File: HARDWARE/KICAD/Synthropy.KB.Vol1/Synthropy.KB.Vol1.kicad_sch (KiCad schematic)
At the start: 1 part, among them U1 kb2040

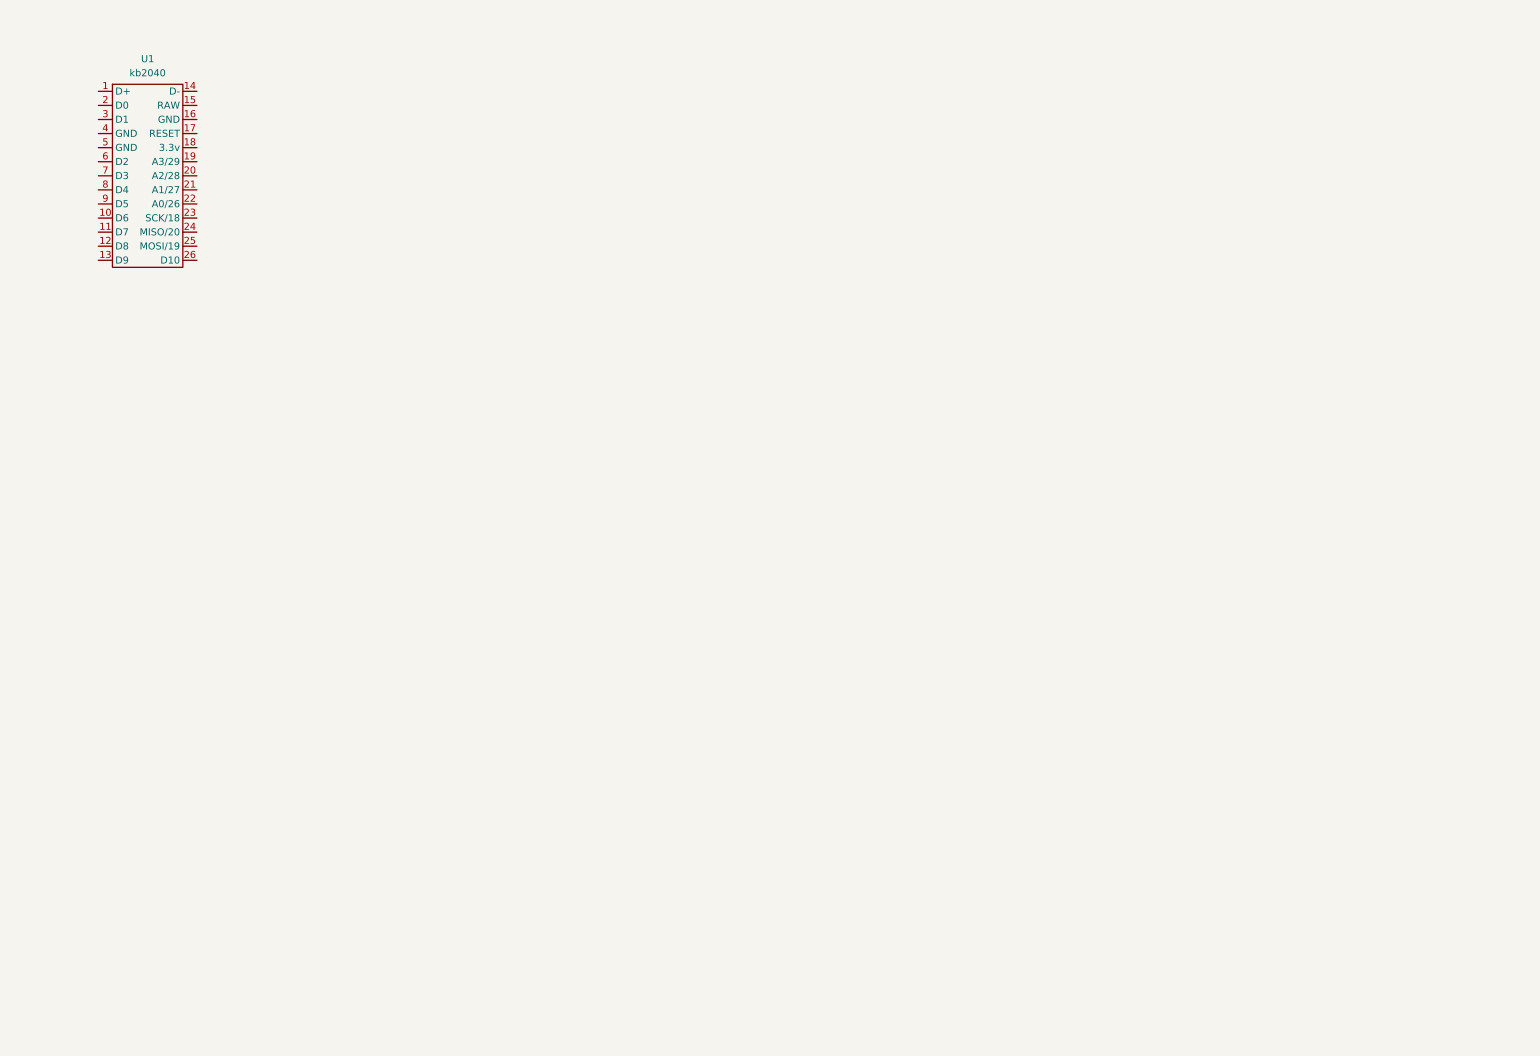
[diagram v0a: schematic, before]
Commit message: Schematic Updates
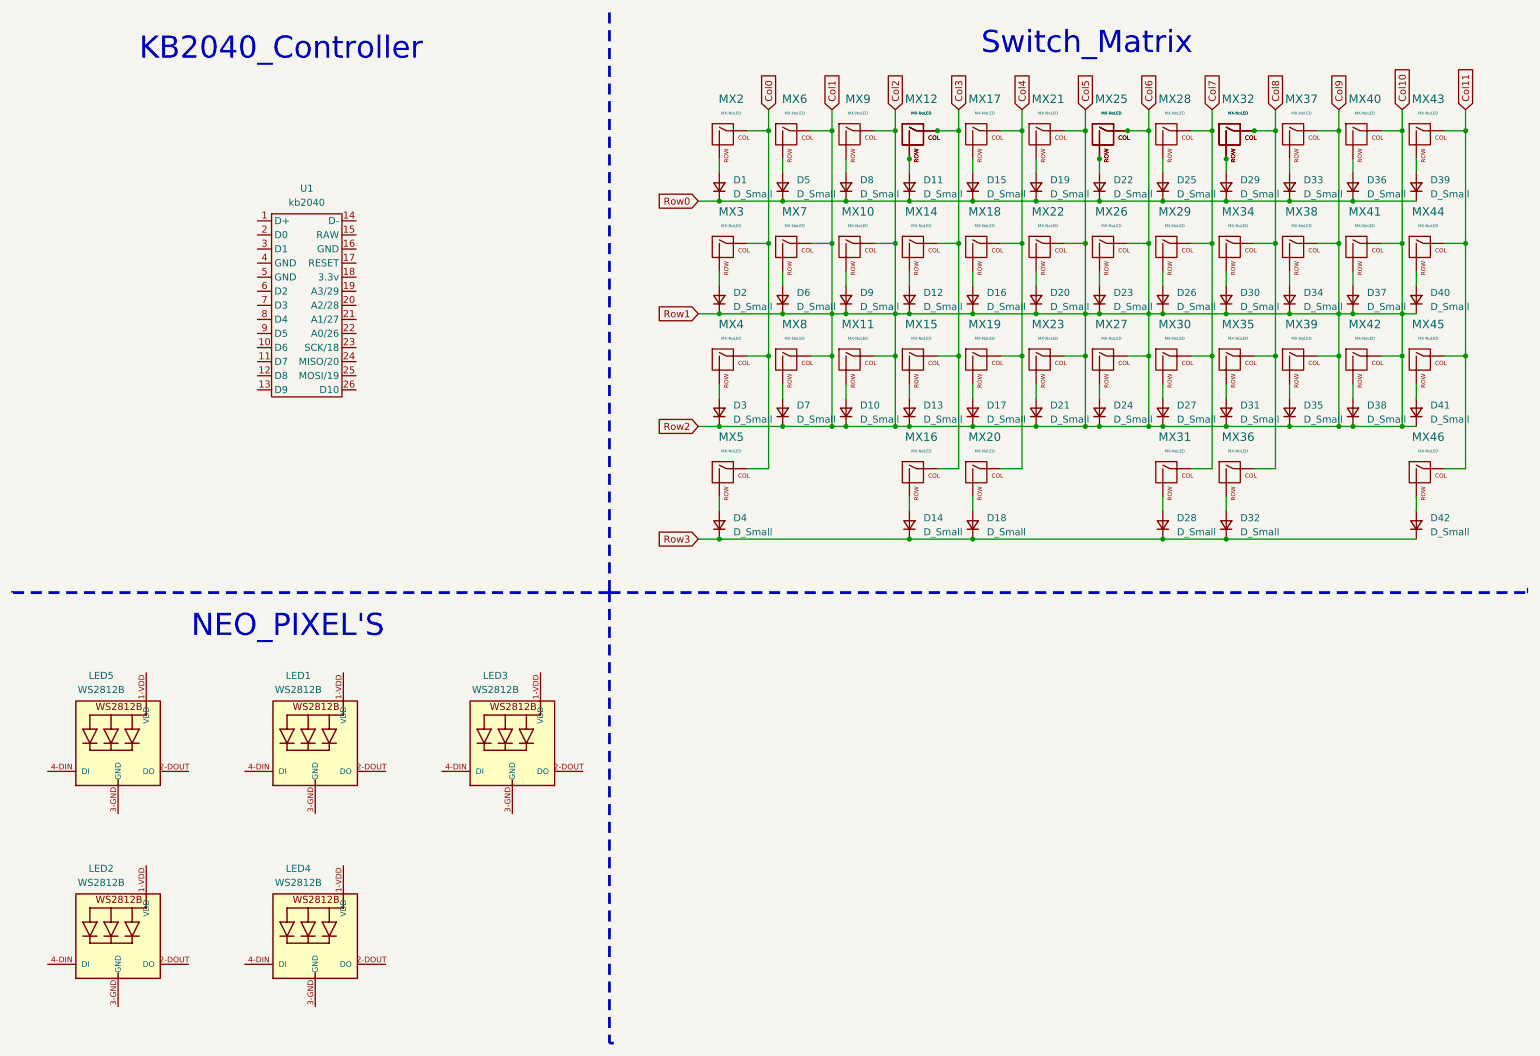
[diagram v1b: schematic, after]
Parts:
- added D1, D10, D11, D12, D13, D14, D15, D16, D17, D18, D19, D2, D20, D21, D22, D23, D24, D25, D26, D27, D28, D29, D3, D30, D31, D32, D33, D34, D35, D36, D37, D38, D39, D4, D40, D41, D42, D5, D6, D7, D8, D9: D_Small, Diode_SMD:D_SOD-123, symbol Device:D_Small
- added LED1, LED2, LED3, LED4, LED5: WS2812B, symbol WS2812B:WS2812B
- added MX10, MX11, MX12, MX13, MX14, MX15, MX16, MX17, MX18, MX19, MX2, MX20, MX21, MX22, MX23, MX24, MX25, MX26, MX27, MX28, MX29, MX3, MX30, MX31, MX32, MX33, MX34, MX35, MX36, MX37, MX38, MX39, MX4, MX40, MX41, MX42, MX43, MX44, MX45, MX46, MX5, MX6, MX7, MX8, MX9: MX-NoLED, Kailh_Switch:Kailh_Choc_SP, symbol MX_Alps_Hybrid:MX-NoLED
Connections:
- new net: D15.2 (A), MX17.2 (ROW)
- new net: D6.2 (A), MX7.2 (ROW)
- new net: D7.2 (A), MX8.2 (ROW)
- new net: D27.2 (A), MX30.2 (ROW)
- new net: D18.2 (A), MX20.2 (ROW)
- new net: D39.2 (A), MX43.2 (ROW)
- new net: D2.2 (A), MX3.2 (ROW)
- new net: D5.2 (A), MX6.2 (ROW)
- new net: D37.2 (A), MX41.2 (ROW)
- new net: D30.2 (A), MX34.2 (ROW)
- new net: D28.2 (A), MX31.2 (ROW)
- new net: D3.2 (A), MX4.2 (ROW)
- new net: D33.2 (A), MX37.2 (ROW)
- new net: D34.2 (A), MX38.2 (ROW)
- new net: D16.2 (A), MX18.2 (ROW)
- new net: D38.2 (A), MX42.2 (ROW)
- new net: D40.2 (A), MX44.2 (ROW)
- new net: D17.2 (A), MX19.2 (ROW)
- new net: D29.2 (A), MX32.2 (ROW), MX33.2 (ROW)
- new net: D11.2 (A), MX12.2 (ROW), MX13.2 (ROW)
- new net: D42.2 (A), MX46.2 (ROW)
- new net: D32.2 (A), MX36.2 (ROW)
- new net: D35.2 (A), MX39.2 (ROW)
- new net: D22.2 (A), MX24.2 (ROW), MX25.2 (ROW)
- new net: D26.2 (A), MX29.2 (ROW)
- new net: D4.2 (A), MX5.2 (ROW)
- new net: D12.2 (A), MX14.2 (ROW)
- new net: D20.2 (A), MX22.2 (ROW)
- new net: D9.2 (A), MX10.2 (ROW)
- new net: D8.2 (A), MX9.2 (ROW)
- new net: D41.2 (A), MX45.2 (ROW)
- new net: D36.2 (A), MX40.2 (ROW)
- new net: D13.2 (A), MX15.2 (ROW)
- new net: D31.2 (A), MX35.2 (ROW)
- new net: D24.2 (A), MX27.2 (ROW)
- new net: D1.2 (A), MX2.2 (ROW)
- new net: D10.2 (A), MX11.2 (ROW)
- new net: D14.2 (A), MX16.2 (ROW)
- new net: D19.2 (A), MX21.2 (ROW)
- new net: D25.2 (A), MX28.2 (ROW)
- new net: D21.2 (A), MX23.2 (ROW)
- new net: D23.2 (A), MX26.2 (ROW)
- new net Col0: MX2.1 (COL), MX3.1 (COL), MX4.1 (COL), MX5.1 (COL)
- new net Col1: D10.1 (K), D12.1 (K), D13.1 (K), D16.1 (K), D17.1 (K), D2.1 (K), D20.1 (K), D21.1 (K), D23.1 (K), D24.1 (K), D26.1 (K), D27.1 (K), D3.1 (K), D30.1 (K), D31.1 (K), D34.1 (K), D35.1 (K), D37.1 (K), D38.1 (K), D40.1 (K), D41.1 (K), D6.1 (K), D7.1 (K), D9.1 (K), MX10.1 (COL), MX11.1 (COL), MX21.1 (COL), MX22.1 (COL), MX23.1 (COL), MX24.1 (COL), MX25.1 (COL), MX26.1 (COL), MX27.1 (COL), MX37.1 (COL), MX38.1 (COL), MX39.1 (COL), MX40.1 (COL), MX41.1 (COL), MX42.1 (COL), MX6.1 (COL), MX7.1 (COL), MX8.1 (COL), MX9.1 (COL)
- new net Col11: MX43.1 (COL), MX44.1 (COL), MX45.1 (COL), MX46.1 (COL)
- new net Col3: MX12.1 (COL), MX13.1 (COL), MX14.1 (COL), MX15.1 (COL), MX16.1 (COL)
- new net Col4: MX17.1 (COL), MX18.1 (COL), MX19.1 (COL), MX20.1 (COL)
- new net Col7: MX28.1 (COL), MX29.1 (COL), MX30.1 (COL), MX31.1 (COL)
- new net Col8: MX32.1 (COL), MX33.1 (COL), MX34.1 (COL), MX35.1 (COL), MX36.1 (COL)
- new net Row0: D1.1 (K), D11.1 (K), D15.1 (K), D19.1 (K), D22.1 (K), D25.1 (K), D29.1 (K), D33.1 (K), D36.1 (K), D39.1 (K), D5.1 (K), D8.1 (K)
- new net Row3: D14.1 (K), D18.1 (K), D28.1 (K), D32.1 (K), D4.1 (K), D42.1 (K)
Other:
- note added: "KB2040_Controller"
- note added: "NEO_PIXEL'S"
- note added: "Switch_Matrix"
- moved on the sheet: U1

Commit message: Updates from prev revisions
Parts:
- removed MX12, MX25, MX33: MX-NoLED, Kailh_Switch:Kailh_Choc_SP, symbol MX_Alps_Hybrid:MX-NoLED
- LED1: renamed from LED5; footprint (none) -> Keebio-Parts.pretty-master:WS2812B
- LED2: renamed from LED3; footprint (none) -> Keebio-Parts.pretty-master:WS2812B
- LED3: renamed from LED2; footprint (none) -> Keebio-Parts.pretty-master:WS2812B
- LED4: footprint (none) -> Keebio-Parts.pretty-master:WS2812B
- LED5: renamed from LED1; footprint (none) -> Keebio-Parts.pretty-master:WS2812B
- MX1: renamed from MX2; footprint Kailh_Switch:Kailh_Choc_SP -> Switch_Keyboard_Kailh:SW_Kailh_Choc_V1V2_1.00u
- MX10: renamed from MX37; footprint Kailh_Switch:Kailh_Choc_SP -> Switch_Keyboard_Kailh:SW_Kailh_Choc_V1V2_1.00u
- MX11: renamed from MX40; footprint Kailh_Switch:Kailh_Choc_SP -> Switch_Keyboard_Kailh:SW_Kailh_Choc_V1V2_1.00u
- MX12: renamed from MX43; footprint Kailh_Switch:Kailh_Choc_SP -> Switch_Keyboard_Kailh:SW_Kailh_Choc_V1V2_1.00u
- MX13: renamed from MX3; footprint Kailh_Switch:Kailh_Choc_SP -> Switch_Keyboard_Kailh:SW_Kailh_Choc_V1V2_1.00u
- MX14: renamed from MX7; footprint Kailh_Switch:Kailh_Choc_SP -> Switch_Keyboard_Kailh:SW_Kailh_Choc_V1V2_1.00u
- MX15: renamed from MX10; footprint Kailh_Switch:Kailh_Choc_SP -> Switch_Keyboard_Kailh:SW_Kailh_Choc_V1V2_1.00u
- MX16: renamed from MX14; footprint Kailh_Switch:Kailh_Choc_SP -> Switch_Keyboard_Kailh:SW_Kailh_Choc_V1V2_1.00u
- MX17: renamed from MX18; footprint Kailh_Switch:Kailh_Choc_SP -> Switch_Keyboard_Kailh:SW_Kailh_Choc_V1V2_1.00u
- MX18: renamed from MX22; footprint Kailh_Switch:Kailh_Choc_SP -> Switch_Keyboard_Kailh:SW_Kailh_Choc_V1V2_1.00u
- MX19: renamed from MX26; footprint Kailh_Switch:Kailh_Choc_SP -> Switch_Keyboard_Kailh:SW_Kailh_Choc_V1V2_1.00u
- MX2: renamed from MX6; footprint Kailh_Switch:Kailh_Choc_SP -> Switch_Keyboard_Kailh:SW_Kailh_Choc_V1V2_1.00u
- MX20: renamed from MX29; footprint Kailh_Switch:Kailh_Choc_SP -> Switch_Keyboard_Kailh:SW_Kailh_Choc_V1V2_1.00u
- MX21: renamed from MX34; footprint Kailh_Switch:Kailh_Choc_SP -> Switch_Keyboard_Kailh:SW_Kailh_Choc_V1V2_1.00u
- MX22: renamed from MX38; footprint Kailh_Switch:Kailh_Choc_SP -> Switch_Keyboard_Kailh:SW_Kailh_Choc_V1V2_1.00u
- MX23: renamed from MX41; footprint Kailh_Switch:Kailh_Choc_SP -> Switch_Keyboard_Kailh:SW_Kailh_Choc_V1V2_1.00u
- MX24: renamed from MX44; footprint Kailh_Switch:Kailh_Choc_SP -> Switch_Keyboard_Kailh:SW_Kailh_Choc_V1V2_1.00u
- MX25: renamed from MX4; footprint Kailh_Switch:Kailh_Choc_SP -> Switch_Keyboard_Kailh:SW_Kailh_Choc_V1V2_1.00u
- MX26: renamed from MX8; footprint Kailh_Switch:Kailh_Choc_SP -> Switch_Keyboard_Kailh:SW_Kailh_Choc_V1V2_1.00u
- MX27: renamed from MX11; footprint Kailh_Switch:Kailh_Choc_SP -> Switch_Keyboard_Kailh:SW_Kailh_Choc_V1V2_1.00u
- MX28: renamed from MX15; footprint Kailh_Switch:Kailh_Choc_SP -> Switch_Keyboard_Kailh:SW_Kailh_Choc_V1V2_1.00u
- MX29: renamed from MX19; footprint Kailh_Switch:Kailh_Choc_SP -> Switch_Keyboard_Kailh:SW_Kailh_Choc_V1V2_1.00u
- MX3: renamed from MX9; footprint Kailh_Switch:Kailh_Choc_SP -> Switch_Keyboard_Kailh:SW_Kailh_Choc_V1V2_1.00u
- MX30: renamed from MX23; footprint Kailh_Switch:Kailh_Choc_SP -> Switch_Keyboard_Kailh:SW_Kailh_Choc_V1V2_1.00u
- MX31: renamed from MX27; footprint Kailh_Switch:Kailh_Choc_SP -> Switch_Keyboard_Kailh:SW_Kailh_Choc_V1V2_1.00u
- MX32: renamed from MX30; footprint Kailh_Switch:Kailh_Choc_SP -> Switch_Keyboard_Kailh:SW_Kailh_Choc_V1V2_1.00u
- MX33: renamed from MX35; footprint Kailh_Switch:Kailh_Choc_SP -> Switch_Keyboard_Kailh:SW_Kailh_Choc_V1V2_1.00u
- MX34: renamed from MX39; footprint Kailh_Switch:Kailh_Choc_SP -> Switch_Keyboard_Kailh:SW_Kailh_Choc_V1V2_1.00u
- MX35: renamed from MX42; footprint Kailh_Switch:Kailh_Choc_SP -> Switch_Keyboard_Kailh:SW_Kailh_Choc_V1V2_1.00u
- MX36: renamed from MX45; footprint Kailh_Switch:Kailh_Choc_SP -> Switch_Keyboard_Kailh:SW_Kailh_Choc_V1V2_1.00u
- MX37: renamed from MX5; footprint Kailh_Switch:Kailh_Choc_SP -> Switch_Keyboard_Kailh:SW_Kailh_Choc_V1V2_1.00u
- MX38: renamed from MX16; footprint Kailh_Switch:Kailh_Choc_SP -> Switch_Keyboard_Kailh:SW_Kailh_Choc_V1V2_1.00u
- MX39: renamed from MX20; footprint Kailh_Switch:Kailh_Choc_SP -> Switch_Keyboard_Kailh:SW_Kailh_Choc_V1V2_1.00u
- MX4: renamed from MX13; footprint Kailh_Switch:Kailh_Choc_SP -> Switch_Keyboard_Kailh:SW_Kailh_Choc_V1V2_1.00u
- MX40: renamed from MX31; footprint Kailh_Switch:Kailh_Choc_SP -> Switch_Keyboard_Kailh:SW_Kailh_Choc_V1V2_1.00u
- MX41: renamed from MX36; footprint Kailh_Switch:Kailh_Choc_SP -> Switch_Keyboard_Kailh:SW_Kailh_Choc_V1V2_1.00u
- MX42: renamed from MX46; footprint Kailh_Switch:Kailh_Choc_SP -> Switch_Keyboard_Kailh:SW_Kailh_Choc_V1V2_1.00u
- MX5: renamed from MX17; footprint Kailh_Switch:Kailh_Choc_SP -> Switch_Keyboard_Kailh:SW_Kailh_Choc_V1V2_1.00u
- MX6: renamed from MX21; footprint Kailh_Switch:Kailh_Choc_SP -> Switch_Keyboard_Kailh:SW_Kailh_Choc_V1V2_1.00u
- MX7: renamed from MX24; footprint Kailh_Switch:Kailh_Choc_SP -> Switch_Keyboard_Kailh:SW_Kailh_Choc_V1V2_1.00u
- MX8: renamed from MX28; footprint Kailh_Switch:Kailh_Choc_SP -> Switch_Keyboard_Kailh:SW_Kailh_Choc_V1V2_1.00u
- MX9: renamed from MX32; footprint Kailh_Switch:Kailh_Choc_SP -> Switch_Keyboard_Kailh:SW_Kailh_Choc_V1V2_1.00u
- U1: footprint (none) -> Pro-Micro:Pro-Micro
- renumbered D33 to D10, D36 to D11, D39 to D12, D2 to D13, D6 to D14, D9 to D15, D12 to D16, D16 to D17, D20 to D18, D23 to D19, D5 to D2, D26 to D20, D30 to D21, D34 to D22, D37 to D23, D40 to D24, D3 to D25, D7 to D26, D10 to D27, D13 to D28, D17 to D29, D8 to D3, D21 to D30, D24 to D31, D27 to D32, D31 to D33, D35 to D34, D38 to D35, D41 to D36, D4 to D37, D14 to D38, D18 to D39, D11 to D4, D28 to D40, D32 to D41, D15 to D5, D19 to D6, D22 to D7, D25 to D8, D29 to D9
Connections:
- net +3V3: now reaches LED1.1-VDD (VDD)
- net +3V3: now also LED2.1-VDD (VDD), LED5.1-VDD (VDD)
- net GND: now reaches LED1.3-GND (GND)
- net GND: now also LED2.3-GND (GND), LED3.3-GND (GND), LED4.3-GND (GND), LED5.3-GND (GND)
- net LED1: now reaches LED1.4-DIN (DI)
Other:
- moved on the sheet: LED1, LED2, LED3, LED4, LED5
